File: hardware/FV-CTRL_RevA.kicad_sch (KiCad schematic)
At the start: 69 parts, among them J1 12V_IN, J10 IR_RX2, J11 IR_TX1 (Col 1), J12 IR_TX2 (Col 2), J13 LS1 (DNP), J14 LS2 (DNP), J15 LS3 (DNP), J16 LS4 (DNP), J17 I2C_RESERVED, J18 ESP32_Left (Pins 1-19), J19 ESP32_Right (Pins 20-38), J2 XH-M401 (6.0V 8A), J3 AUX_BUCK (DNP), J4 MP1584EN (5V Logic), J5 S1_TOP, J6 S1_BOT, J7 S2_TOP, J8 S2_BOT, J9 IR_RX1, Q1 IRF9540N, Q2 S8050

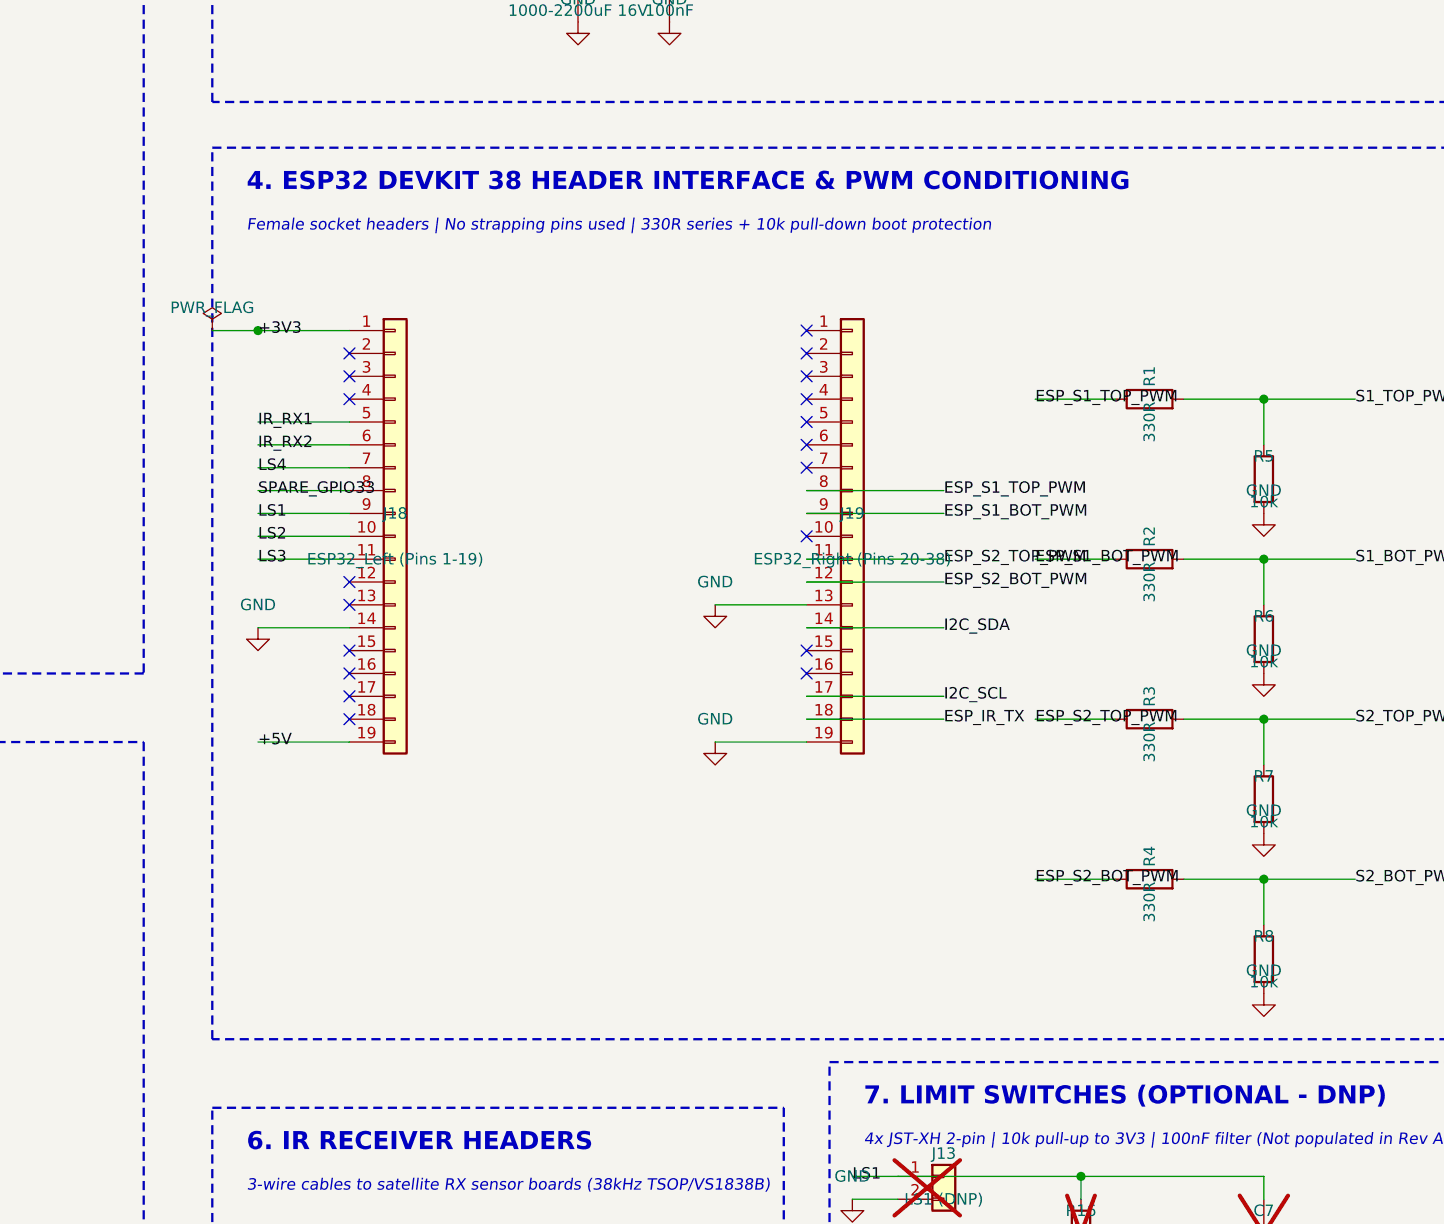
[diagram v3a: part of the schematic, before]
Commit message: feat(sch): migrate ESP32 to SMD module, add AMS1117-3.3 LDO subsystem, and expansion sensor headers
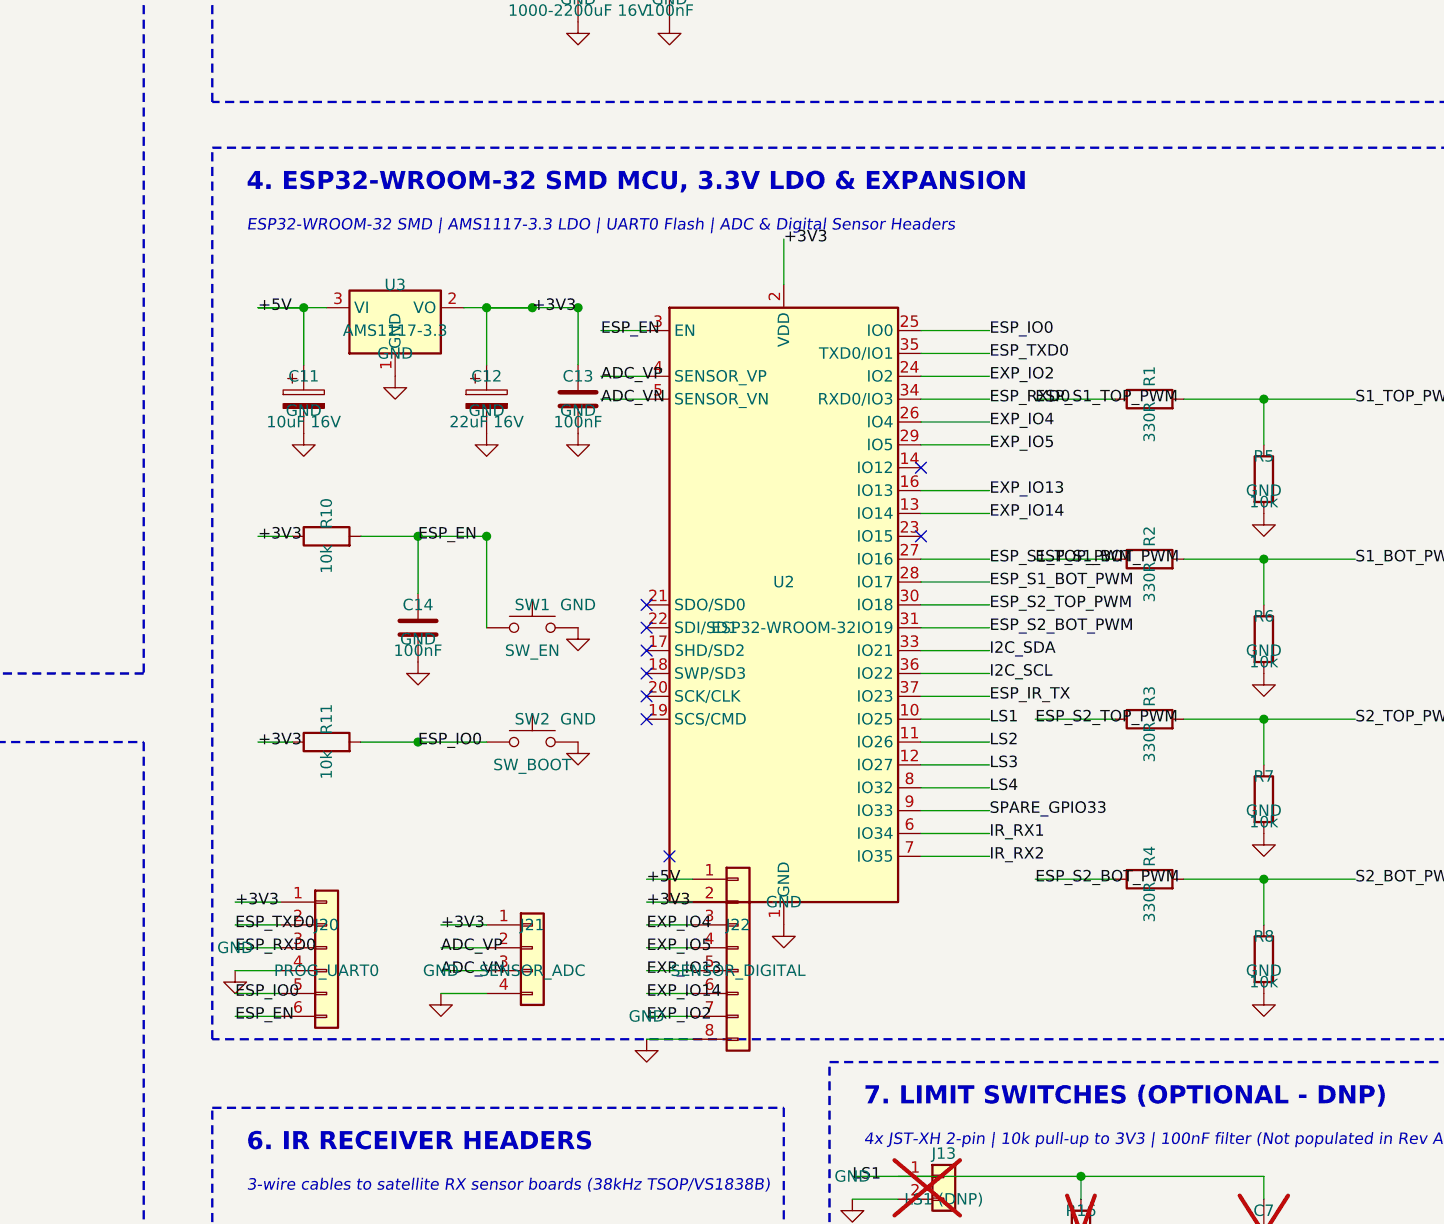
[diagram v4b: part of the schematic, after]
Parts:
- removed J18: ESP32_Left (Pins 1-19), Connector_PinSocket_2.54mm:PinSocket_1x19_P2.54mm_Vertical, symbol Connector_Generic:Conn_01x19
- removed J19: ESP32_Right (Pins 20-38), Connector_PinSocket_2.54mm:PinSocket_1x19_P2.54mm_Vertical, symbol Connector_Generic:Conn_01x19
- added C11: 10uF 16V, Capacitor_THT:CP_Radial_D5.0mm_P2.00mm, symbol Device:C_Polarized
- added C12: 22uF 16V, Capacitor_THT:CP_Radial_D5.0mm_P2.00mm, symbol Device:C_Polarized
- added C13, C14: 100nF, Capacitor_THT:C_Disc_D5.0mm_W2.5mm_P5.00mm, symbol Device:C
- added J20: PROG_UART0, Connector_PinHeader_2.54mm:PinHeader_1x06_P2.54mm_Vertical, symbol Connector_Generic:Conn_01x06
- added J21: SENSOR_ADC, Connector_PinHeader_2.54mm:PinHeader_1x04_P2.54mm_Vertical, symbol Connector_Generic:Conn_01x04
- added J22: SENSOR_DIGITAL, Connector_PinHeader_2.54mm:PinHeader_1x08_P2.54mm_Vertical, symbol Connector_Generic:Conn_01x08
- added R10, R11: 10k, Resistor_THT:R_Axial_DIN0207_L6.3mm_D2.5mm_P7.62mm_Horizontal, symbol Device:R
- added SW1: SW_EN, Button_Switch_THT:SW_PUSH_6mm_H5mm, symbol Switch:SW_Push
- added SW2: SW_BOOT, Button_Switch_THT:SW_PUSH_6mm_H5mm, symbol Switch:SW_Push
- added U2: ESP32-WROOM-32, RF_Module:ESP32-WROOM-32, symbol RF_Module:ESP32-WROOM-32
- added U3: AMS1117-3.3, Package_TO_SOT_SMD:SOT-223-3_TabPin2, symbol Regulator_Linear:AP1117-15
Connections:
- net +3V3: now also C12.1, C13.1, J20.1 (Pin_1), J21.1 (Pin_1), J22.2 (Pin_2), R10.1, R11.1, U2.2 (VDD), U3.2 (VO)
- net +5V: now also C11.1, J22.1 (Pin_1), U3.3 (VI)
- net ESP_IR_TX: now also U2.37 (IO23)
- net ESP_S1_BOT_PWM: now also U2.28 (IO17)
- net ESP_S1_TOP_PWM: now also U2.27 (IO16)
- net ESP_S2_BOT_PWM: now also U2.31 (IO19)
- net ESP_S2_TOP_PWM: now also U2.30 (IO18)
- net GND: now also C11.2, C12.2, C13.2, C14.2, J20.4 (Pin_4), J21.4 (Pin_4), J22.8 (Pin_8), SW1.2, SW2.2, U2.1 (GND), U2.15 (GND), U2.38 (GND), U2.39 (GND), U3.1 (GND)
- net I2C_SCL: now also U2.36 (IO22)
- net I2C_SDA: now also U2.33 (IO21)
- net IR_RX1: now also U2.6 (IO34)
- net IR_RX2: now also U2.7 (IO35)
- net LS1: now also U2.10 (IO25)
- net LS2: now also U2.11 (IO26)
- net LS3: now also U2.12 (IO27)
- net LS4: now also U2.8 (IO32)
- net SPARE_GPIO33: now also U2.9 (IO33)
- new net ADC_VN: J21.3 (Pin_3), U2.5 (SENSOR_VN)
- new net ADC_VP: J21.2 (Pin_2), U2.4 (SENSOR_VP)
- new net ESP_EN: C14.1, J20.6 (Pin_6), R10.2, SW1.1, U2.3 (EN)
- new net ESP_IO0: J20.5 (Pin_5), R11.2, SW2.1, U2.25 (IO0)
- new net ESP_RXD0: J20.3 (Pin_3), U2.34 (RXD0/IO3)
- new net ESP_TXD0: J20.2 (Pin_2), U2.35 (TXD0/IO1)
- new net EXP_IO13: J22.5 (Pin_5), U2.16 (IO13)
- new net EXP_IO14: J22.6 (Pin_6), U2.13 (IO14)
- new net EXP_IO2: J22.7 (Pin_7), U2.24 (IO2)
- new net EXP_IO4: J22.3 (Pin_3), U2.26 (IO4)
- new net EXP_IO5: J22.4 (Pin_4), U2.29 (IO5)
- no-connect marks 19 -> 9
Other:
- note added: "4. ESP32-WROOM-32 SMD MCU, 3.3V LDO & EXPANSION"
- note added: "ESP32-WROOM-32 SMD | AMS1117-3.3 LDO | UART0 Flash | ADC & Digital Sensor Headers"
- note removed: "4. ESP32 DEVKIT 38 HEADER INTERFACE & PWM CONDITIONING"
- note removed: "Female socket headers | No strapping pins used | 330R series + 10k pull-down boot protection"
